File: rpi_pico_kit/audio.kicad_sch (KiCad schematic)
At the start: 37 parts, among them J13 AudioJack-CUI-SJ-3523-SMT, J14 AudioJack-CUI-SJ-3523-SMT, Q7 DMN63D8L-7, U10 74LVC2G34GV, U11 PCM5101A, U9 NCP115-3.3_SOT23-5

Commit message: added 3D models, repaired SSD1306 footprint
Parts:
- U10: footprint Package_SO:SC-74-6_1.5x2.9mm_P0.95mm -> Package_SO:TSOP-6_1.65x3.05mm_P0.95mm
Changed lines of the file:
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@@
       (effects (font (size 1.27 1.27)))
     )
-    (property "Footprint" "Package_SO:SC-74-6_1.5x2.9mm_P0.95mm" (id 2) (at 53.34 49.53 0)
+    (property "Footprint" "Package_SO:TSOP-6_1.65x3.05mm_P0.95mm" (id 2) (at 53.34 49.53 0)
       (effects (font (size 1.27 1.27)) hide)
     )

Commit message: changed footprint for THT jumpers to use jumper 3D model
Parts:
- JP19: footprint Connector_PinHeader_2.54mm:PinHeader_1x02_P2.54mm_Vertical -> JumperTHT:JumperTHT_2_P2.54mm_Open
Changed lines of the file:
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@@
       (effects (font (size 1.27 1.27)))
     )
-    (property "Footprint" "Connector_PinHeader_2.54mm:PinHeader_1x02_P2.54mm_Vertical" (id 2) (at 219.71 114.3 0)
+    (property "Footprint" "JumperTHT:JumperTHT_2_P2.54mm_Open" (id 2) (at 219.71 114.3 0)
       (effects (font (size 1.27 1.27)) hide)
     )

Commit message: changed footprints from 0805 to 0603
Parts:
- C31, C32, C34, C36, C38, C40, C44: footprint Capacitor_SMD:C_0805_2012Metric_Pad1.18x1.45mm_HandSolder -> Capacitor_SMD:C_0603_1608Metric_Pad1.08x0.95mm_HandSolder; Supplier Part URL https://www.digikey.cz/en/products/detail/kemet/C0805C104M3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 -> (none)
- C45, C46: footprint Capacitor_SMD:C_0805_2012Metric_Pad1.18x1.45mm_HandSolder -> Capacitor_SMD:C_0603_1608Metric_Pad1.08x0.95mm_HandSolder; Supplier Part URL https://www.digikey.cz/en/products/detail/kemet/C0805C222K5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 -> (none)
- R100, R101, R92, R93, R94, R95, R96, R97, R98, R99: footprint Resistor_SMD:R_0805_2012Metric_Pad1.20x1.40mm_HandSolder -> Resistor_SMD:R_0603_1608Metric_Pad0.98x0.95mm_HandSolder; Supplier Part URL https://www.digikey.cz/en/products/detail/yageo/RC0805FR-07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 -> (none)

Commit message: changed footprint U10
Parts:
- U10: footprint Package_SO:TSOP-6_1.65x3.05mm_P0.95mm -> Package_SO:SC-74-6_1.5x2.9mm_P0.95mm
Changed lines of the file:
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@@
       (effects (font (size 1.27 1.27)))
     )
-    (property "Footprint" "Package_SO:TSOP-6_1.65x3.05mm_P0.95mm" (id 2) (at 53.34 49.53 0)
+    (property "Footprint" "Package_SO:SC-74-6_1.5x2.9mm_P0.95mm" (id 2) (at 53.34 49.53 0)
       (effects (font (size 1.27 1.27)) hide)
     )

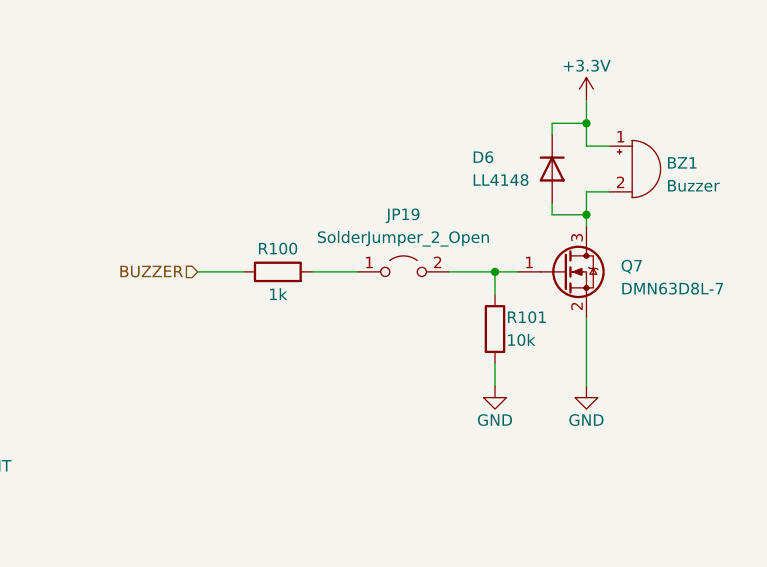
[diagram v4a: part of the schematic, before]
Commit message: monostable leds (unrouted 99)
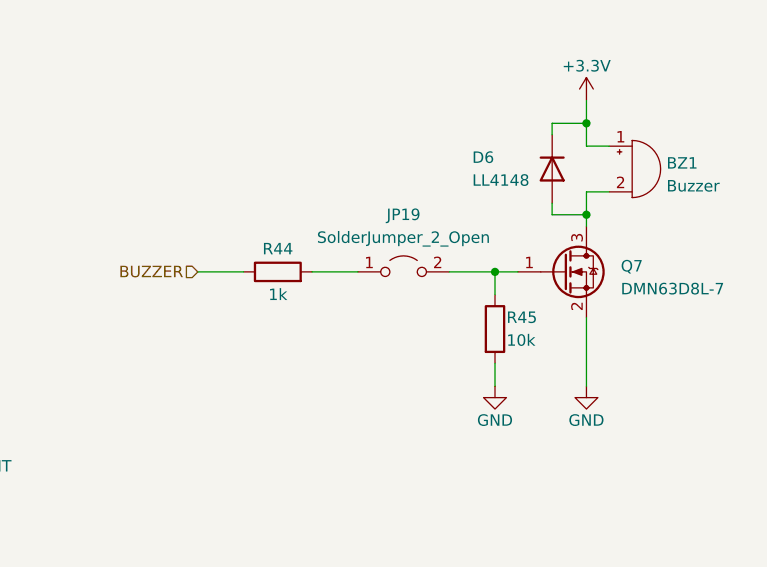
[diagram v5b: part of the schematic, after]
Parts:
- renumbered R100 to R44, R101 to R45
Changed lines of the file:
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@@
   (symbol (lib_id "Device:R") (at 205.74 114.3 90) (unit 1)
     (in_bom yes) (on_board yes)
-    (property "Reference" "R100" (id 0) (at 205.74 111.76 90)
+    (property "Reference" "R44" (id 0) (at 205.74 111.76 90)
       (effects (font (size 1.27 1.27)))
     )
@@
     )
     (property "Manufacturer Part Number" "RC0805FR-071KL" (id 4) (at 205.74 114.3 0)
-      (effects (font (size 1.27 1.27)) hide)
-    )
-    (property "Supplier Part URL" "" (id 5) (at 205.74 114.3 0)
       (effects (font (size 1.27 1.27)) hide)
     )
@@
   (symbol (lib_id "Device:R") (at 229.87 120.65 0) (unit 1)
     (in_bom yes) (on_board yes)
-    (property "Reference" "R101" (id 0) (at 231.14 119.38 0)
+    (property "Reference" "R45" (id 0) (at 231.14 119.38 0)
       (effects (font (size 1.27 1.27)) (justify left))
     )
@@
       (effects (font (size 1.27 1.27)) hide)
     )
-    (property "Supplier Part URL" "" (id 5) (at 229.87 120.65 0)
-      (effects (font (size 1.27 1.27)) hide)
-    )

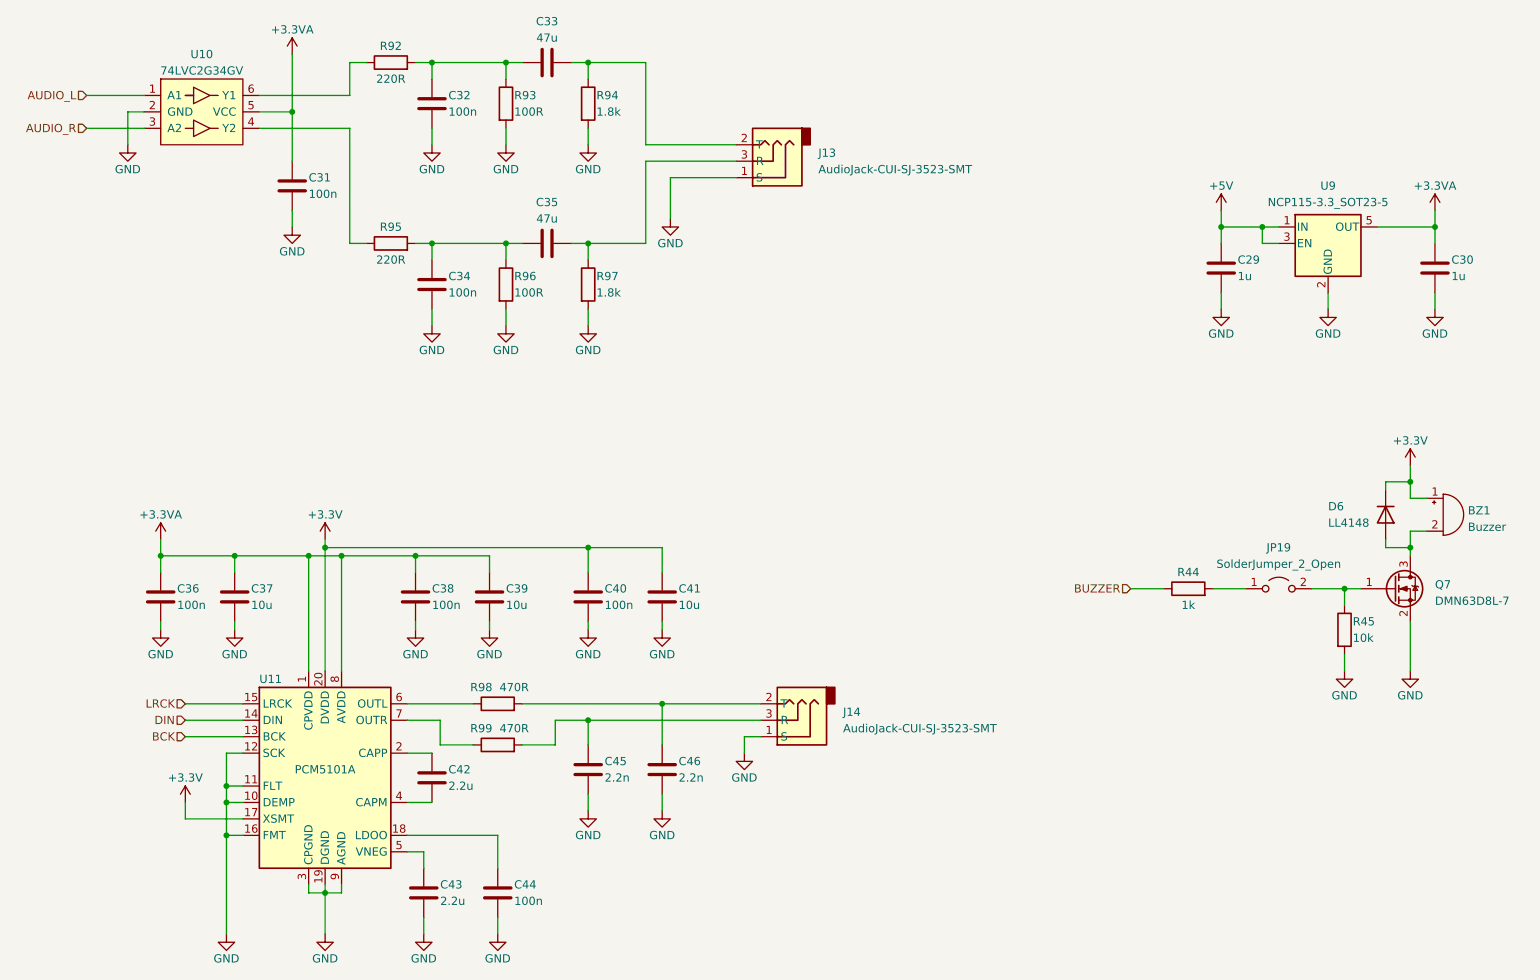
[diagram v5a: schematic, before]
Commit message: schematic cleared annotation
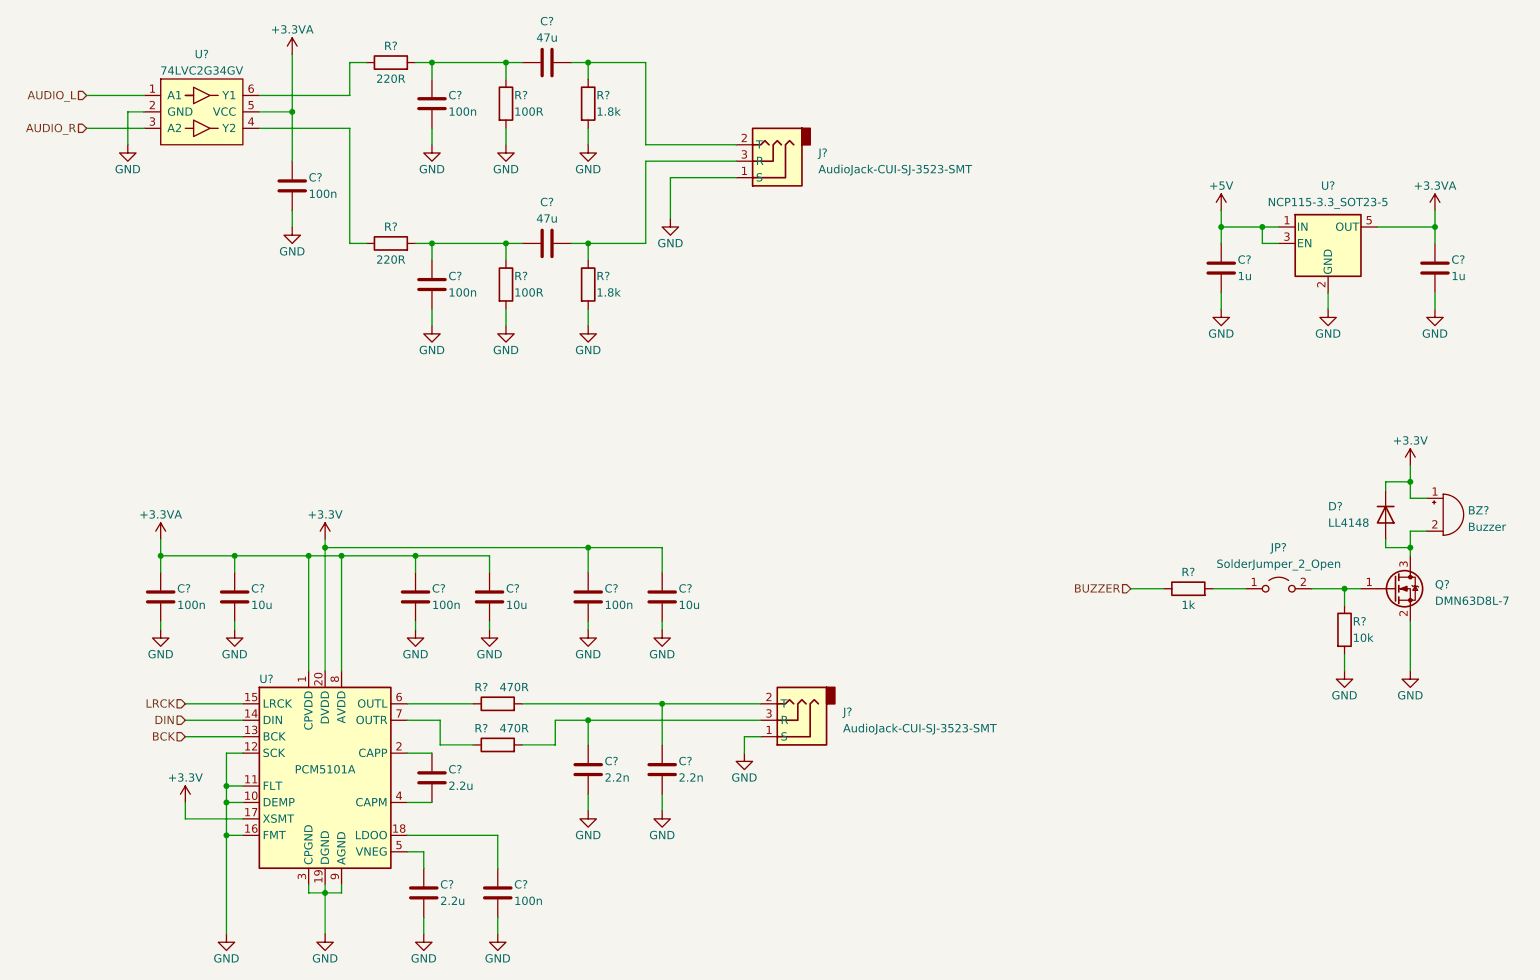
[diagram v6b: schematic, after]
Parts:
- renumbered BZ1 to BZ?, C44 to C?, C40 to C?, C38 to C?, C30 to C?, C45 to C?, C39 to C?, C43 to C?, C42 to C?, C33 to C?, C46 to C?, C37 to C?, C36 to C?, C29 to C?, C32 to C?, C41 to C?, C31 to C?, C34 to C?, C35 to C?, D6 to D?, J13 to J?, J14 to J?, JP19 to JP?, Q7 to Q?, R94 to R?, R44 to R?, R92 to R?, R98 to R?, R97 to R?, R45 to R?, R96 to R?, R99 to R?, R95 to R?, R93 to R?, U9 to U?, U10 to U?, U11 to U?

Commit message: renumbered parts
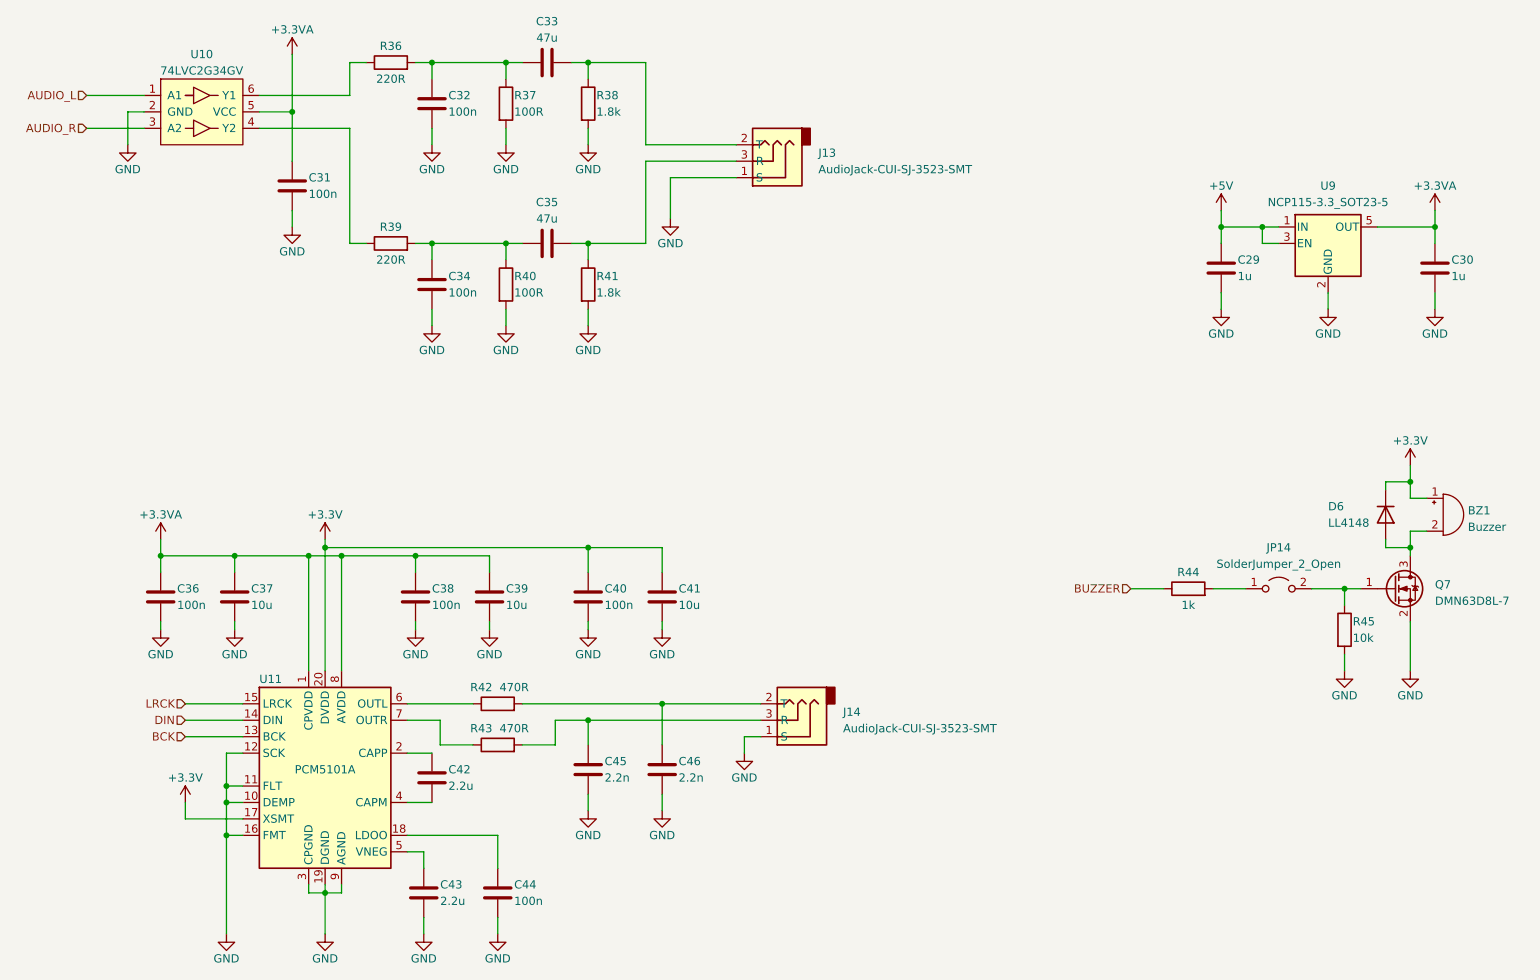
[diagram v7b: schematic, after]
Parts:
- gave numbers to parts that had none: 37
